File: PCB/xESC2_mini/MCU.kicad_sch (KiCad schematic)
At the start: 14 parts, among them U4 STM32F405RGTx, Y1 Crystal_GND24

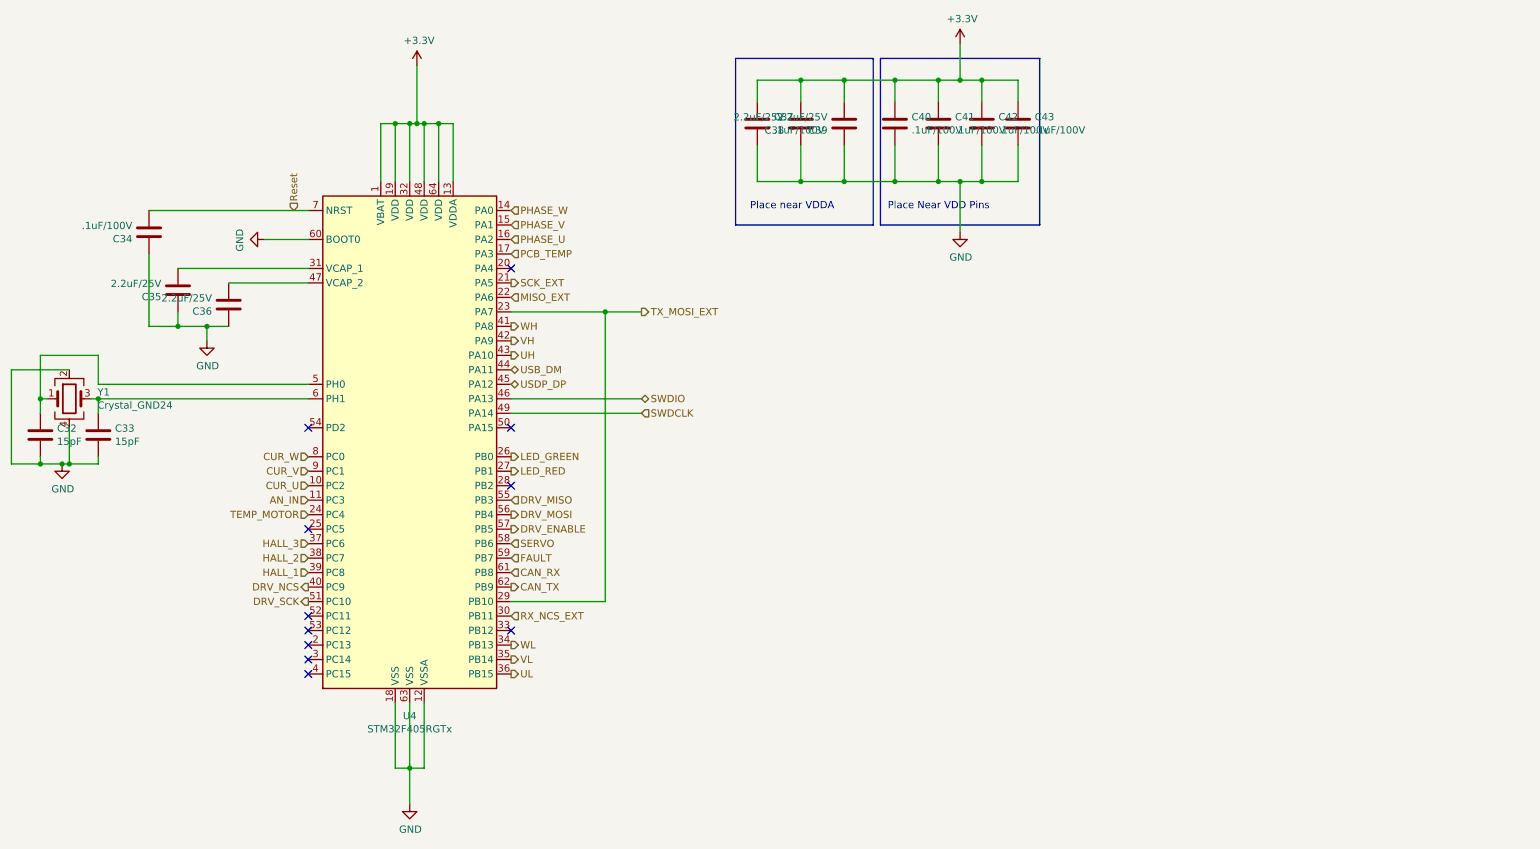
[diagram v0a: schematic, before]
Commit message: wip - start of RP2040 swap in for STM uC - just a rough guess at an IO map
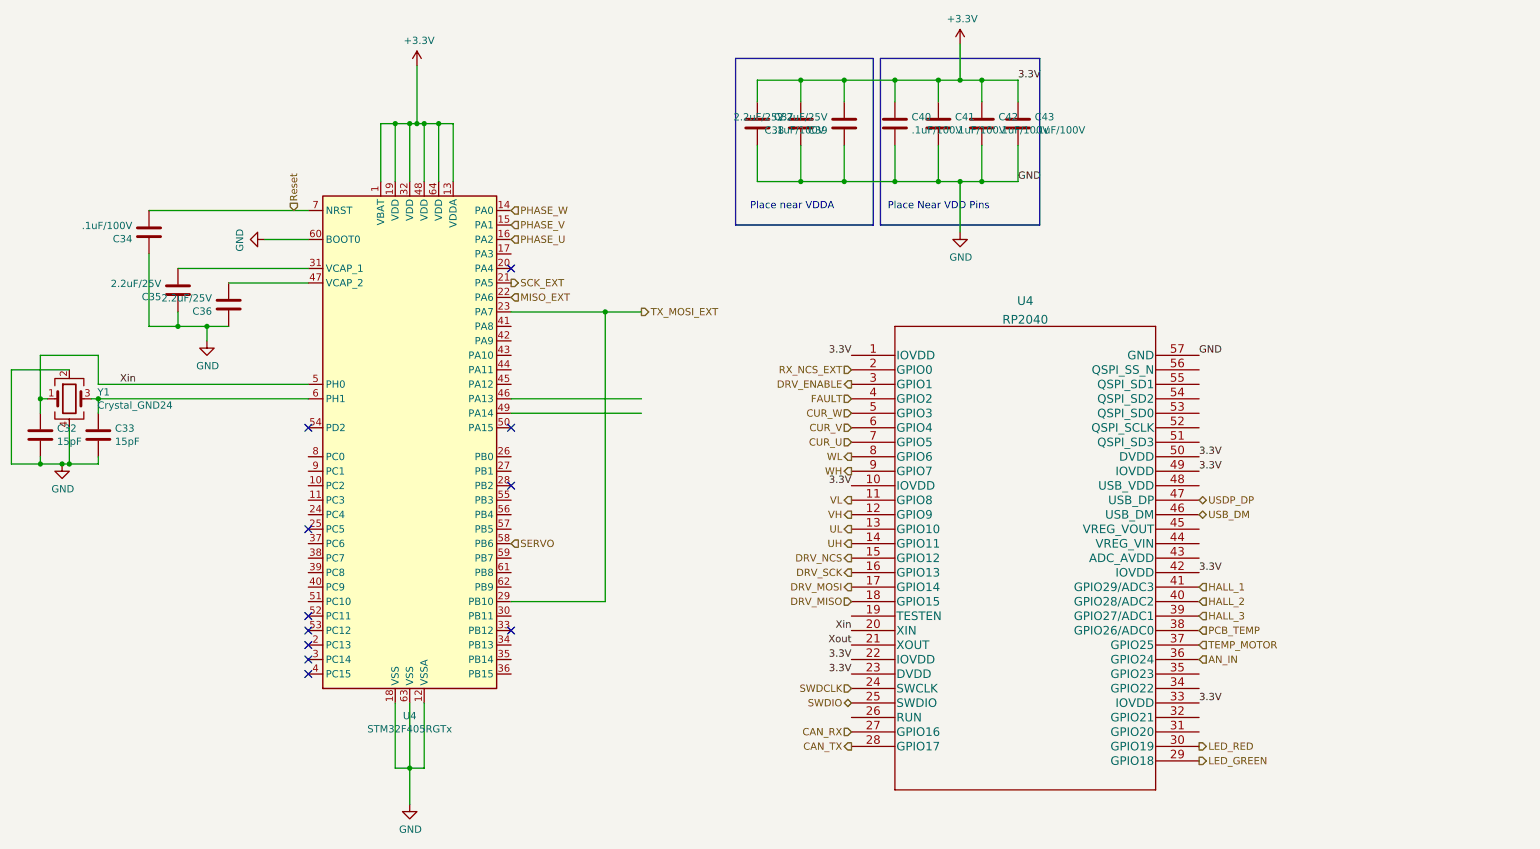
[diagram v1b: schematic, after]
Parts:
- added U4: RP2040, IC57_RP2040, symbol OpenMower:RP2040
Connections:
- net +3V3: now also U4.1 (IOVDD), U4.10 (IOVDD), U4.22 (IOVDD), U4.23 (DVDD), U4.33 (IOVDD), U4.42 (IOVDD), U4.49 (IOVDD), U4.50 (DVDD)
- net AN_IN: now also U4.36 (GPIO24); no longer U4.11 (PC3)
- net CAN_RX: now also U4.27 (GPIO16); no longer U4.61 (PB8)
- net CAN_TX: now also U4.28 (GPIO17); no longer U4.62 (PB9)
- net CUR_U: now also U4.7 (GPIO5); no longer U4.10 (PC2)
- net CUR_V: now also U4.6 (GPIO4); no longer U4.9 (PC1)
- net CUR_W: now also U4.5 (GPIO3); no longer U4.8 (PC0)
- net DRV_ENABLE: now also U4.3 (GPIO1); no longer U4.57 (PB5)
- net DRV_MISO: now also U4.18 (GPIO15); no longer U4.55 (PB3)
- net DRV_MOSI: now also U4.17 (GPIO14); no longer U4.56 (PB4)
- net DRV_NCS: now also U4.15 (GPIO12); no longer U4.40 (PC9)
- net DRV_SCK: now also U4.16 (GPIO13); no longer U4.51 (PC10)
- net FAULT: now also U4.4 (GPIO2); no longer U4.59 (PB7)
- net GND: now also U4.57 (GND)
- net HALL_1: now also U4.41 (GPIO29/ADC3); no longer U4.39 (PC8)
- net HALL_2: now also U4.40 (GPIO28/ADC2); no longer U4.38 (PC7)
- net HALL_3: now also U4.39 (GPIO27/ADC1); no longer U4.37 (PC6)
- net LED_GREEN: now also U4.29 (GPIO18); no longer U4.26 (PB0)
- net LED_RED: now also U4.30 (GPIO19); no longer U4.27 (PB1)
- net PCB_TEMP: now also U4.38 (GPIO26/ADC0); no longer U4.17 (PA3)
- net RX_NCS_EXT: now also U4.2 (GPIO0); no longer U4.30 (PB11)
- net SWDCLK: now also U4.24 (SWCLK); no longer U4.49 (PA14)
- net SWDIO: now also U4.25 (SWDIO); no longer U4.46 (PA13)
- net TEMP_MOTOR: now also U4.37 (GPIO25); no longer U4.24 (PC4)
- net UH: now also U4.14 (GPIO11); no longer U4.43 (PA10)
- net UL: now also U4.13 (GPIO10); no longer U4.36 (PB15)
- net USB_DM: now also U4.46 (USB_DM); no longer U4.44 (PA11)
- net USDP_DP: now also U4.47 (USB_DP); no longer U4.45 (PA12)
- net VH: now also U4.12 (GPIO9); no longer U4.42 (PA9)
- net VL: now also U4.11 (GPIO8); no longer U4.35 (PB14)
- net WH: now also U4.9 (GPIO7); no longer U4.41 (PA8)
- net WL: now also U4.8 (GPIO6); no longer U4.34 (PB13)
- net Xin: now reaches C32.1, U4.5 (PH0), Y1.1
- net Xin: now also U4.20 (XIN)
- new net Xout: U4.21 (XOUT)

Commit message: wip - had not save the pcb with tmp footprint inserted to check routing
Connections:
- net AN_IN: now also U4.38 (GPIO26/ADC0); no longer U4.36 (GPIO24)
- net CAN_RX: now also U4.6 (GPIO4); no longer U4.27 (GPIO16)
- net CAN_TX: now also U4.7 (GPIO5); no longer U4.28 (GPIO17)
- net CUR_U: now also U4.39 (GPIO27/ADC1); no longer U4.7 (GPIO5)
- net CUR_V: now also U4.40 (GPIO28/ADC2); no longer U4.6 (GPIO4)
- net CUR_W: now also U4.41 (GPIO29/ADC3); no longer U4.5 (GPIO3)
- net HALL_1: now also U4.36 (GPIO24); no longer U4.41 (GPIO29/ADC3)
- net HALL_2: now also U4.35 (GPIO23); no longer U4.40 (GPIO28/ADC2)
- net HALL_3: now also U4.34 (GPIO22); no longer U4.39 (GPIO27/ADC1)
- net PCB_TEMP: now also U4.32 (GPIO21); no longer U4.38 (GPIO26/ADC0)
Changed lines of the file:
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@@
     (effects (font (size 1.27 1.27)) (justify right bottom))
   )
-  (hierarchical_label "CAN_TX" (shape output) (at 162.56 138.43 180)
+  (hierarchical_label "CAN_TX" (shape output) (at 162.56 85.09 180)
     (effects (font (size 1.27 1.27)) (justify right))
   )
@@
     (effects (font (size 1.27 1.27)) (justify left))
   )
-  (hierarchical_label "CAN_RX" (shape input) (at 162.56 135.89 180)
+  (hierarchical_label "CAN_RX" (shape input) (at 162.56 82.55 180)
     (effects (font (size 1.27 1.27)) (justify right))
   )
@@
     (effects (font (size 1.27 1.27)) (justify right))
   )
-  (hierarchical_label "CUR_V" (shape input) (at 162.56 82.55 180)
-    (effects (font (size 1.27 1.27)) (justify right))
+  (hierarchical_label "CUR_V" (shape input) (at 223.52 113.03 0)
+    (effects (font (size 1.27 1.27)) (justify left))
   )
   (hierarchical_label "VH" (shape output) (at 162.56 97.79 180)
@@
     (effects (font (size 1.27 1.27)) (justify right))
   )
-  (hierarchical_label "AN_IN" (shape input) (at 223.52 123.19 0)
+  (hierarchical_label "AN_IN" (shape input) (at 223.52 118.11 0)
     (effects (font (size 1.27 1.27)) (justify left))
   )
-  (hierarchical_label "CUR_U" (shape input) (at 162.56 85.09 180)
-    (effects (font (size 1.27 1.27)) (justify right))
+  (hierarchical_label "CUR_U" (shape input) (at 223.52 115.57 0)
+    (effects (font (size 1.27 1.27)) (justify left))
   )
-  (hierarchical_label "PCB_TEMP" (shape input) (at 223.52 118.11 0)
+  (hierarchical_label "PCB_TEMP" (shape input) (at 223.52 133.35 0)
     (effects (font (size 1.27 1.27)) (justify left))
   )
@@
     (effects (font (size 1.27 1.27)) (justify right))
   )
-  (hierarchical_label "HALL_1" (shape input) (at 223.52 110.49 0)
+  (hierarchical_label "HALL_1" (shape input) (at 223.52 123.19 0)
     (effects (font (size 1.27 1.27)) (justify left))
   )
@@
     (effects (font (size 1.27 1.27)) (justify right))
   )
-  (hierarchical_label "CUR_W" (shape input) (at 162.56 80.01 180)
-    (effects (font (size 1.27 1.27)) (justify right))
+  (hierarchical_label "CUR_W" (shape input) (at 223.52 110.49 0)
+    (effects (font (size 1.27 1.27)) (justify left))
   )
   (hierarchical_label "MISO_EXT" (shape input) (at 102.87 59.69 0)
@@
     (effects (font (size 1.27 1.27)) (justify left))
   )
-  (hierarchical_label "HALL_2" (shape input) (at 223.52 113.03 0)
+  (hierarchical_label "HALL_2" (shape input) (at 223.52 125.73 0)
     (effects (font (size 1.27 1.27)) (justify left))
   )
@@
     (effects (font (size 1.27 1.27)) (justify left))
   )
-  (hierarchical_label "HALL_3" (shape input) (at 223.52 115.57 0)
+  (hierarchical_label "HALL_3" (shape input) (at 223.52 128.27 0)
     (effects (font (size 1.27 1.27)) (justify left))
   )

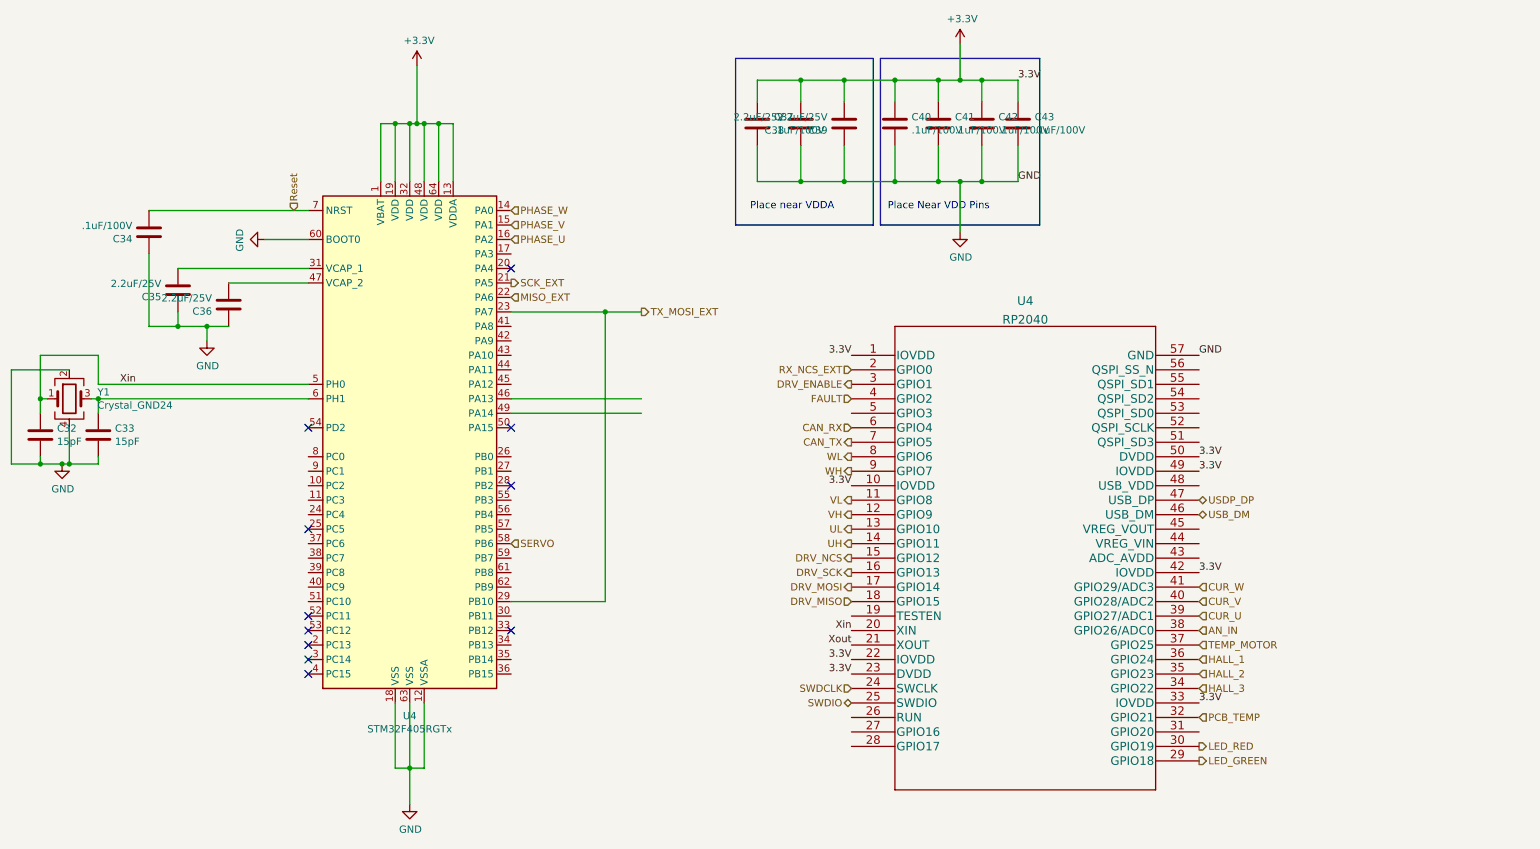
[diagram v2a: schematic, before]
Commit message: wip - most routing for RP2040 done
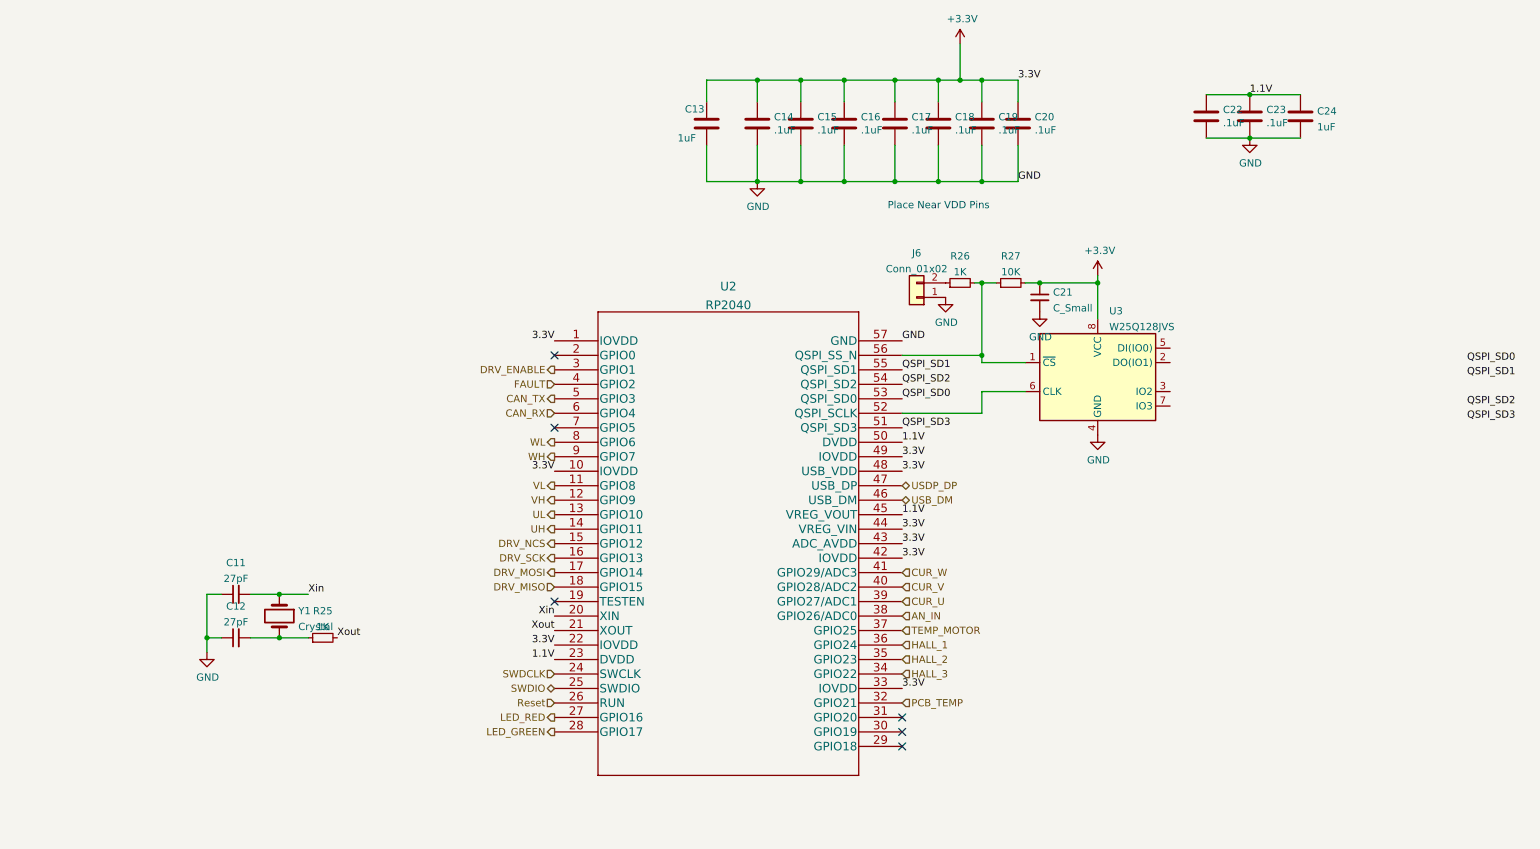
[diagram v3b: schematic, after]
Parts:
- removed C32, C33: 15pF, Capacitor_SMD:C_0603_1608Metric, symbol Device:C
- removed C34: .1uF/100V, Capacitor_SMD:C_0603_1608Metric, symbol Device:C
- removed C35, C36, C38, C39: 2.2uF/25V, Capacitor_SMD:C_0805_2012Metric, symbol Device:C
- removed U4: STM32F405RGTx, Package_QFP:LQFP-64_10x10mm_P0.5mm, symbol MCU_ST_STM32F4:STM32F405RGTx
- removed Y1: Crystal_GND24, Crystal:Crystal_SMD_3225-4Pin_3.2x2.5mm, symbol Device:Crystal_GND24
- added C11, C12: 27pF, Capacitor_SMD:C_0603_1608Metric, symbol Device:C_Small
- added C13, C24: 1uF, Capacitor_SMD:C_0603_1608Metric, symbol Device:C
- added C14, C15, C16, C23: .1uF, Capacitor_SMD:C_0603_1608Metric, symbol Device:C
- added C21: C_Small, symbol Device:C_Small
- added J6: Conn_01x02, Connector_PinHeader_2.54mm:PinHeader_1x02_P2.54mm_Vertical, symbol Connector_Generic:Conn_01x02
- added R25, R26: 1K, Resistor_SMD:R_0603_1608Metric, symbol Device:R_Small
- added R27: 10K, Resistor_SMD:R_0603_1608Metric, symbol Device:R_Small
- added U3: W25Q128JVS, Package_SO:SOIC-8_5.23x5.23mm_P1.27mm, symbol Memory_Flash:W25Q128JVS
- added Y1: Crystal, Crystal:Crystal_SMD_3225-4Pin_3.2x2.5mm, symbol Device:Crystal
- C17: renamed from C40; value .1uF/100V -> .1uF
- C18: renamed from C41; value .1uF/100V -> .1uF
- C19: renamed from C42; value .1uF/100V -> .1uF
- C20: renamed from C43; value .1uF/100V -> .1uF
- C22: renamed from C37; value .1uF/100V -> .1uF
- U2: renamed from U4; footprint IC57_RP2040 -> xESC2:RP2040
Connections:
- net +3V3: now also U2.43 (ADC_AVDD), U2.44 (VREG_VIN), U2.48 (USB_VDD), C13.1, C14.1, C15.1, C16.1, C21.1, R27.2, U3.8 (VCC); no longer C22.1, U2.23 (DVDD), U2.50 (DVDD)
- net CAN_TX: now also U2.5 (GPIO3); no longer U2.7 (GPIO5)
- net GND: now also C11.1, C12.1, C13.2, C14.2, C15.2, C16.2, C21.2, C23.2, C24.2, J6.1 (Pin_1), U3.4 (GND)
- net LED_GREEN: now also U2.28 (GPIO17); no longer U2.29 (GPIO18)
- net LED_RED: now also U2.27 (GPIO16); no longer U2.30 (GPIO19)
- net Reset: now also U2.26 (RUN)
- net Xin: now also C11.2, Y1.1
- net Xout: now also R25.2
- net 1.1V: now reaches U2.45 (VREG_VOUT)
- net 1.1V: now also C22.1, U2.23 (DVDD), U2.50 (DVDD), C23.1, C24.1
- net QSPI_SD3: now reaches U2.51 (QSPI_SD3)
- net at U2.52 (QSPI_SCLK): now also U3.6 (CLK)
- net QSPI_SD0: now reaches U2.53 (QSPI_SD0)
- net QSPI_SD2: now reaches U2.54 (QSPI_SD2)
- net QSPI_SD1: now reaches U2.55 (QSPI_SD1)
- net at U2.56 (QSPI_SS_N): now also R26.2, R27.1, U3.1 (~{CS})
- net RX_NCS_EXT: no longer names the net of U2.2 (GPIO0)
- new net: C12.2, R25.1, Y1.2
- new net: J6.2 (Pin_2), R26.1
- no-connect marks 11 -> 6
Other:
- note removed: "Place near VDDA"
- moved on the sheet: C22, U2

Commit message: wip - landed a couple more bypass caps - 2 left
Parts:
- removed C21: C_Small, symbol Device:C_Small
- Y1: Part Number ABLS-12.000MHZ-B4-T -> (none)
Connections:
- net QSPI_SD0: now also U3.5 (DI(IO0))
- net QSPI_SD1: now also U3.2 (DO(IO1))
- net QSPI_SD2: now also U3.3 (IO2)
- net QSPI_SD3: now also U3.7 (IO3)
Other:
- moved on the sheet: U3
